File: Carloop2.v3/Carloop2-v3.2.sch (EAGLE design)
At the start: 30 parts, among them IC1 RT8258, IC2 AZ1117E, IC3 TJA1049, IC4 MCP2517FD, IC5 PARTICLE_MESH_SMTDUAL, J1 OBDII, Q1 40MHz

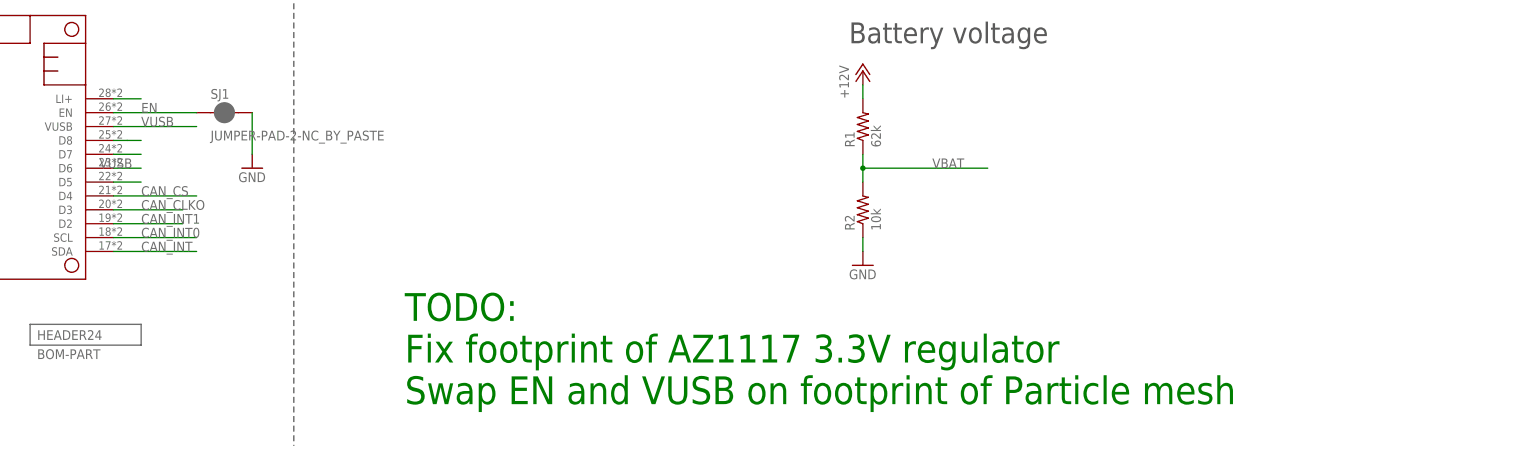
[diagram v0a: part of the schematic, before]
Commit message: Fix PCB bugs
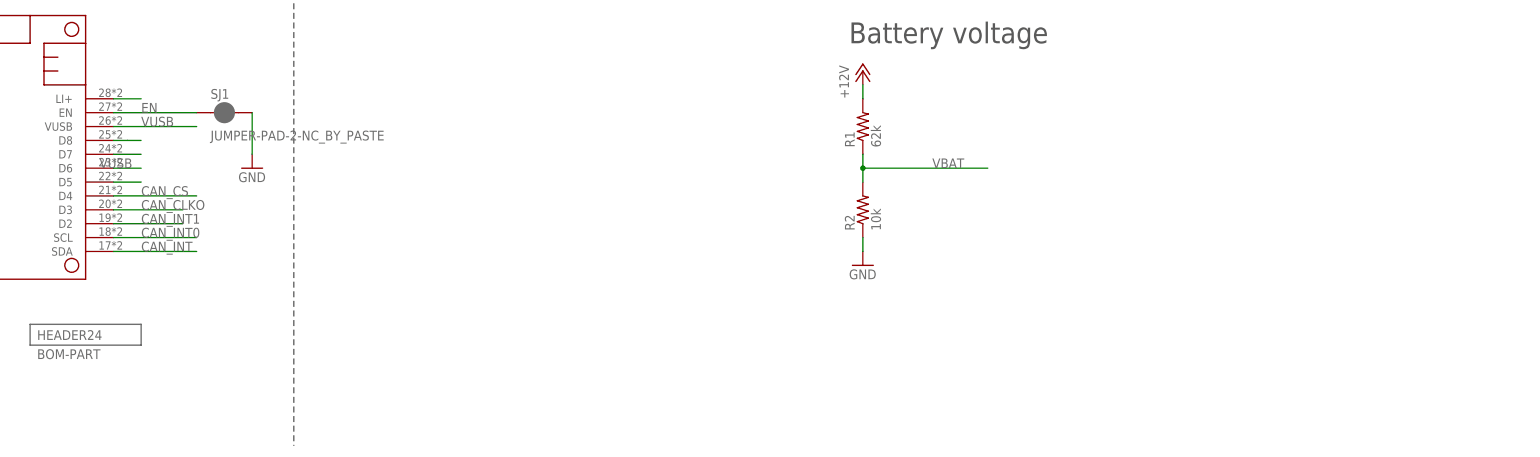
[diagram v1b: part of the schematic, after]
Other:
- note removed: "TODO: Fix footprint of AZ1117 3.3V regulator Swap EN and VUSB on footprint of Particle mesh"
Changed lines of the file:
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@@
 <text x="195.58" y="160.02" size="3.81" layer="97">CAN Transceiver</text>
 <text x="10.16" y="81.28" size="1.778" layer="97">Replace by AP2112 (LDO 5V to 3.3V)</text>
-<text x="137.16" y="-7.62" size="5.08" layer="91">TODO:
-Fix footprint of AZ1117 3.3V regulator
-Swap EN and VUSB on footprint of Particle mesh</text>
 </plain>
 <instances>
@@
 </drawing>
 <compatibility>
-<note version="6.3" minversion="6.2.2" severity="warning">
-Since Version 6.2.2 text objects can contain more than one line,
-which will not be processed correctly with this version.
-</note>
 <note version="8.2" severity="warning">
 Since Version 8.2, EAGLE supports online libraries. The ids
